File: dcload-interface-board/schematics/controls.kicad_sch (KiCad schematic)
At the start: 15 parts, among them SW500 KLS TS6604B, SW501 KLS TS6604B, SW502 KLS TS6604B, SW503 KLS TS6604B, SW504 KLS TS6604B, SW505 KLS TS6604B, SW506 PEC11R-4220F-S24

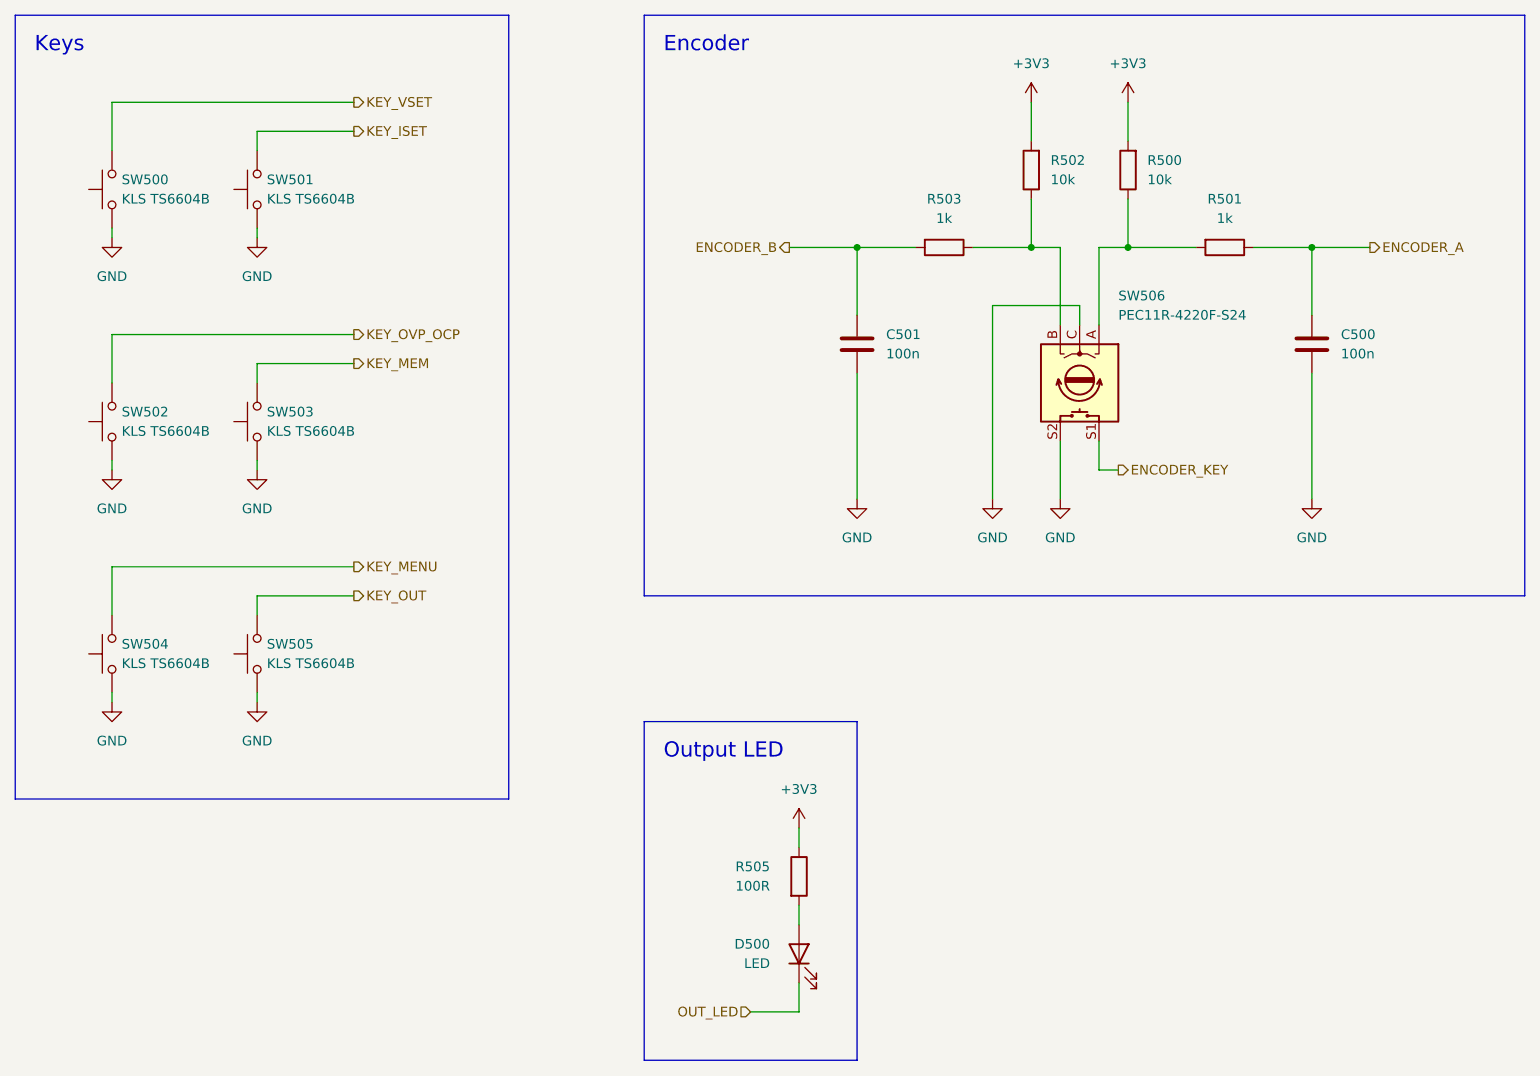
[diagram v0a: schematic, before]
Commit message: add: interface panel board
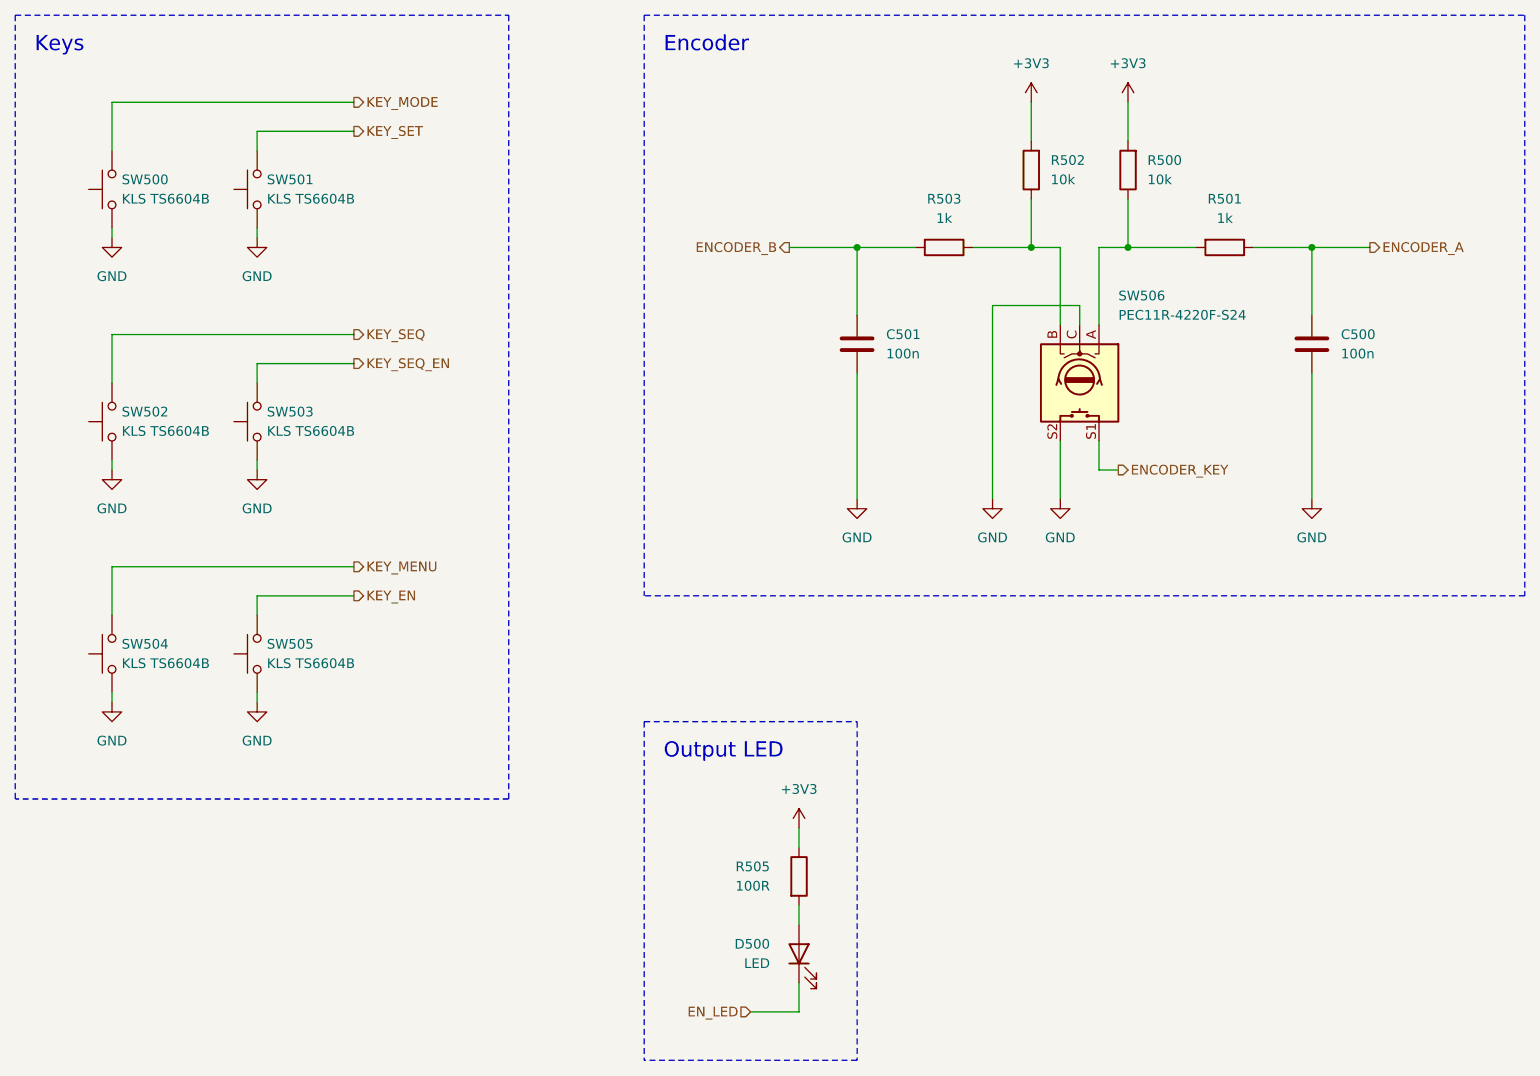
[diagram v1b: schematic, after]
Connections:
- net KEY_ISET renamed KEY_SET
- net KEY_MEM renamed KEY_SEQ_EN
- net KEY_OUT renamed KEY_EN
- net KEY_OVP_OCP renamed KEY_SEQ
- net KEY_VSET renamed KEY_MODE
- net OUT_LED renamed EN_LED
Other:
- title: Linear PSU Digital Board -> Controls
